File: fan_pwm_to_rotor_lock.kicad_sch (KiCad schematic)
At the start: 12 parts, among them J1 Conn_01x04, J2 Conn_01x04, U1 LM393

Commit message: update
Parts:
- added C3: 100n, Capacitor_SMD:C_0805_2012Metric_Pad1.18x1.45mm_HandSolder, symbol Device:C
- added H1, H2: MountingHole_Pad, MountingHole:MountingHole_3.2mm_M3_Pad_Via, symbol Mechanical:MountingHole_Pad
- U1: footprint easyeda2kicad:MINISO-8_L3.0-W3.0-P0.65-LS4.9-BL -> Package_SO:SSOP-8_2.95x2.8mm_P0.65mm
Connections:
- net GND: now also C3.2
- net VDD: now also R1.2, C3.1; no longer R1.1
- net passthrough: now reaches J2.4 (Pin_4)
- net passthrough: now also J1.4 (Pin_4)
- net at D2.2, J1.1 (Pin_1), R3.1: now also R1.1; no longer R1.2
- no-connect marks 1 -> 3

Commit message: kaliva ton pairneis
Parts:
- removed H2: MountingHole_Pad, MountingHole:MountingHole_3.2mm_M3_Pad_Via, symbol Mechanical:MountingHole_Pad
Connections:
- no-connect marks 3 -> 2
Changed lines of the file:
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@@
-	)
-	(no_connect
-		(at 187.96 102.87)
 	)
 	(no_connect
@@
 	(label "passthrough"
 		(at 55.88 62.23 0)
+		(fields_autoplaced yes)
 		(effects
 			(font
@@
 	(label "passthrough"
 		(at 163.83 50.8 0)
+		(fields_autoplaced yes)
 		(effects
 			(font
@@
 					(unit 1)
 				)
-			)
-		)
-	)
-	(symbol
-		(lib_id "Mechanical:MountingHole_Pad")
-		(at 187.96 100.33 0)
-		(unit 1)
-		(exclude_from_sim yes)
-		(in_bom no)
-		(on_board yes)
-		(dnp no)
-		(fields_autoplaced yes)
-		(property "Reference" "H2"
-			(at 190.5 97.7899 0)
-			(effects
-				(font
-					(size 1.27 1.27)
-				)
-				(justify left)
-			)
-		)
-		(property "Value" "MountingHole_Pad"
-			(at 190.5 100.3299 0)
-			(effects
-				(font
-					(size 1.27 1.27)
-				)
-				(justify left)
-			)
-		)
-		(property "Footprint" "MountingHole:MountingHole_3.2mm_M3_Pad_Via"
-			(at 187.96 100.33 0)
-			(effects
-				(font
-					(size 1.27 1.27)
-				)
-				(hide yes)
-			)
-		)
-		(property "Datasheet" "~"
-			(at 187.96 100.33 0)
-			(effects
-				(font
-					(size 1.27 1.27)
-				)
-				(hide yes)
-			)
-		)
-		(property "Description" "Mounting Hole with connection"
-			(at 187.96 100.33 0)
-			(effects
-				(font
-					(size 1.27 1.27)
-				)
-				(hide yes)
-			)
-		)
-		(pin "1"
-		)
-		(instances
-			(project "fan_pwm_to_rotor_lock"
-				(path "/ea79ce20-436b-47a0-b861-e37296079d12"
-					(reference "H2")
-					(unit 1)
-				)

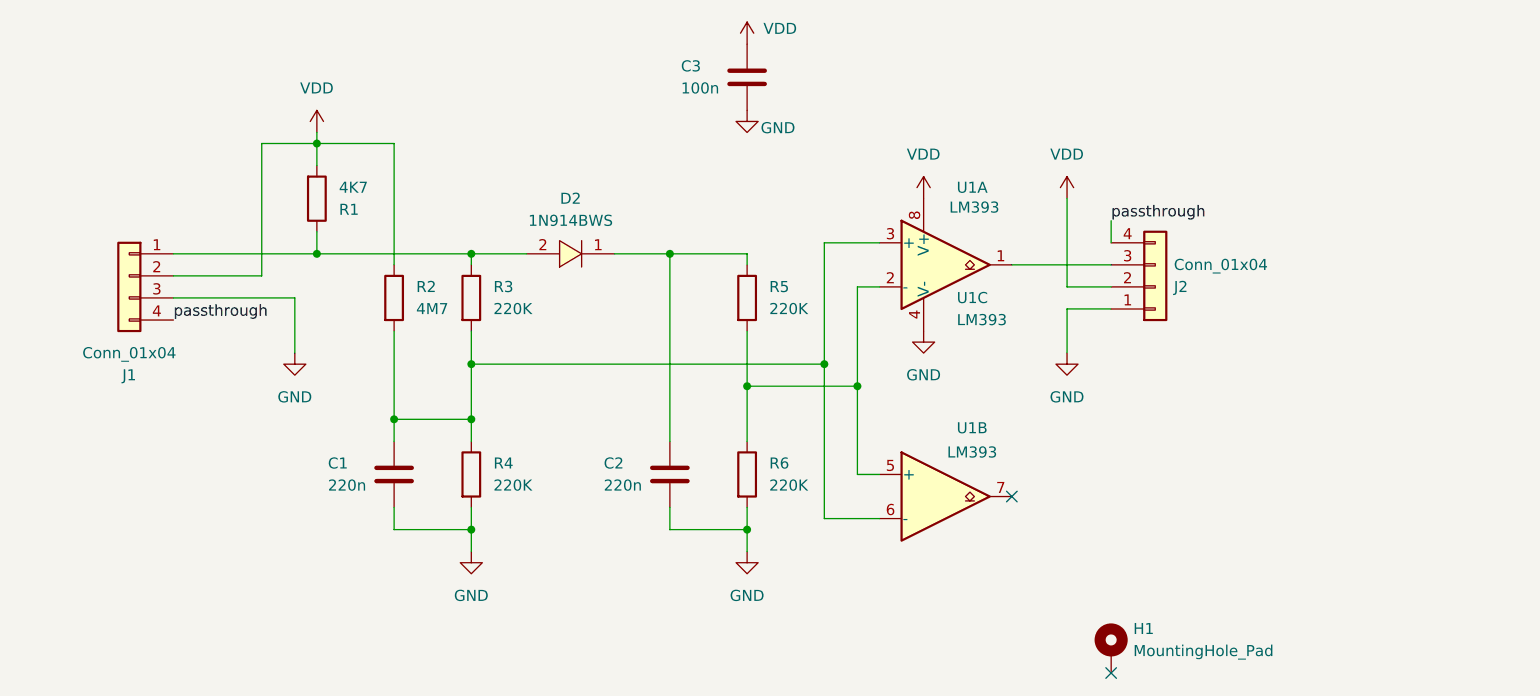
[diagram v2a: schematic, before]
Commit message: Fix incorrect pin assignment
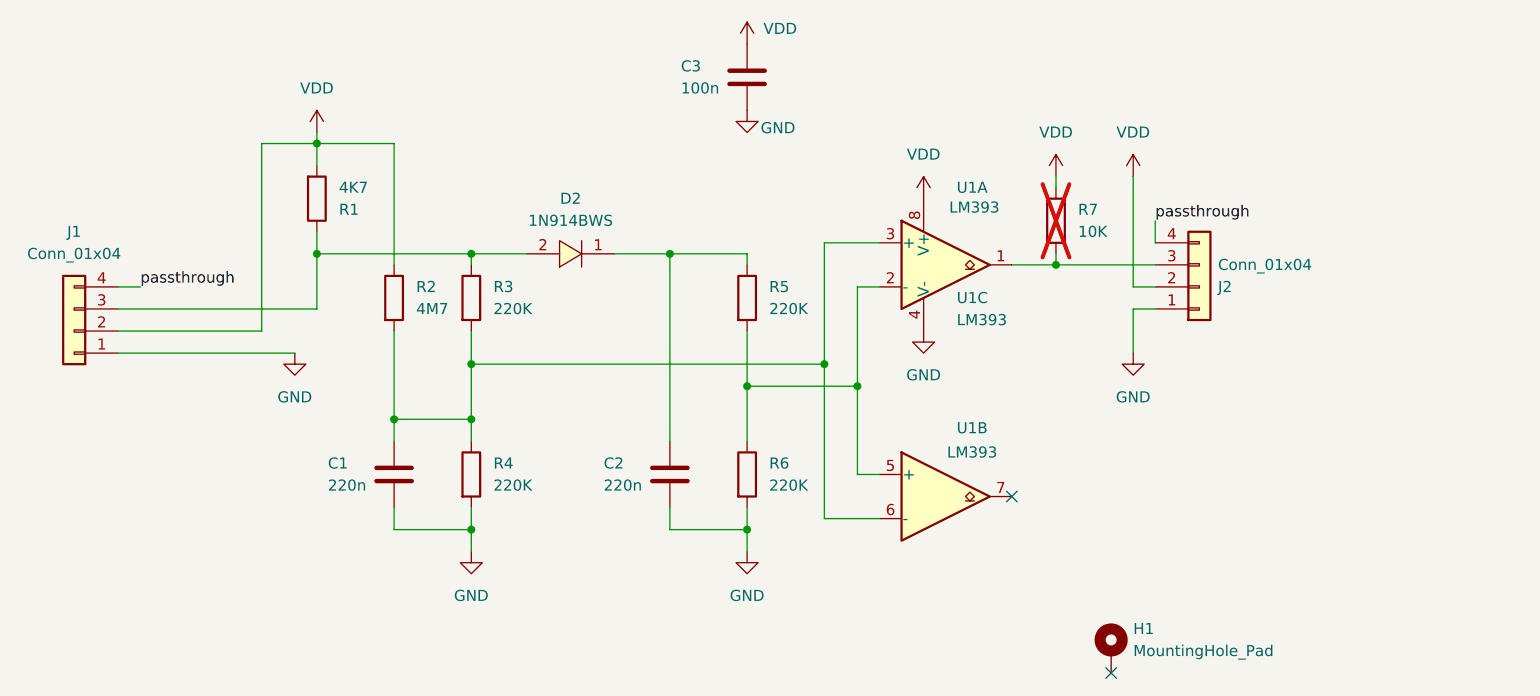
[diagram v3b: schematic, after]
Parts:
- added R7: 10K, Resistor_SMD:R_0805_2012Metric_Pad1.20x1.40mm_HandSolder, symbol Device:R
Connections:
- net GND: now also J1.1 (Pin_1); no longer J1.3 (Pin_3)
- net VDD: now also R7.1
- net at J2.3 (Pin_3), U1.1: now also R7.2
- net at D2.2, R1.1, R3.1: now also J1.3 (Pin_3); no longer J1.1 (Pin_1)
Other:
- moved on the sheet: J1, J2
